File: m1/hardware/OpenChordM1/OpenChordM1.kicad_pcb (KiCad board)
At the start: 4 copper layers, 119 x 63.1 mm, 75 parts, among them J1 TYPE-C-31-M-12, J2 SJ1-3523N (OUT), J3 SJ1-3523N (IN), SW1 SW_Gateron_LP, SW10 EVQPUC02K, SW11 EVQPUC02K, SW13 TS-1187A-B-A-B, SW2 SW_Gateron_LP, SW3 SW_Gateron_LP, SW4 SW_Gateron_LP, SW5 SW_Gateron_LP, SW6 SW_Gateron_LP, SW7 SW_Gateron_LP, SW8 SW_Gateron_LP, SW9 EVQPUC02K, U1 RP2040, U2 CT_Slider_Chev_3_74d5_15_noESD, U3 IQS572-BL-QNR, U4 AT42QT2120-XUR, U5 CT_Trackpad_7x7_37D75, U6 W25Q32JVSSIQ, U7 AP2112K-3.3TRG1, U8 USBLC6-2SC6, U9 TLP2361, Y1 ABM8-272-T3

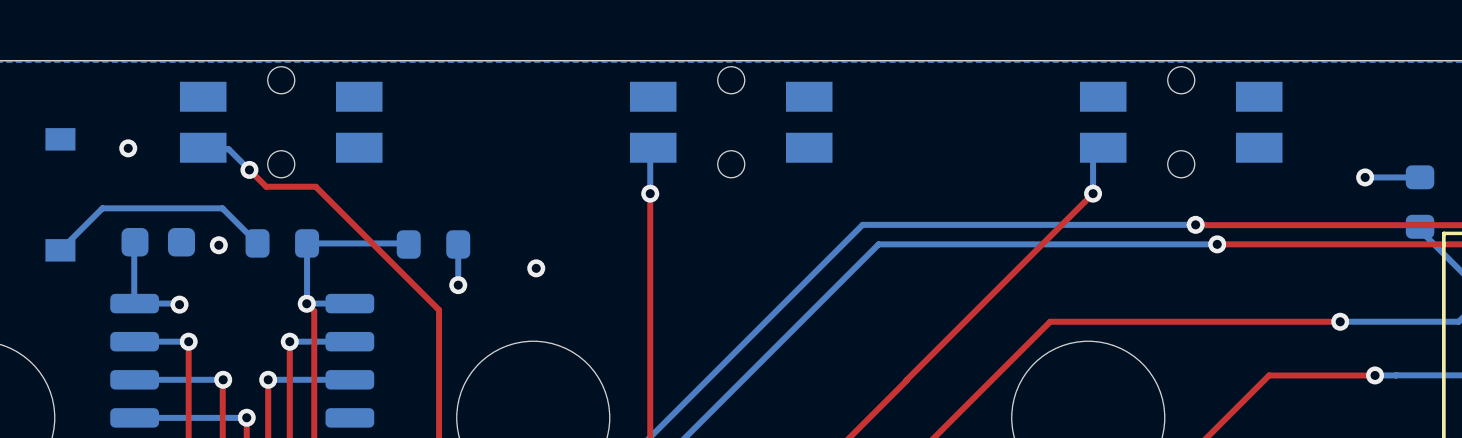
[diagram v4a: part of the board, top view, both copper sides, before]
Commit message: Save USB-C pair routing and a board STEP for the enclosure.
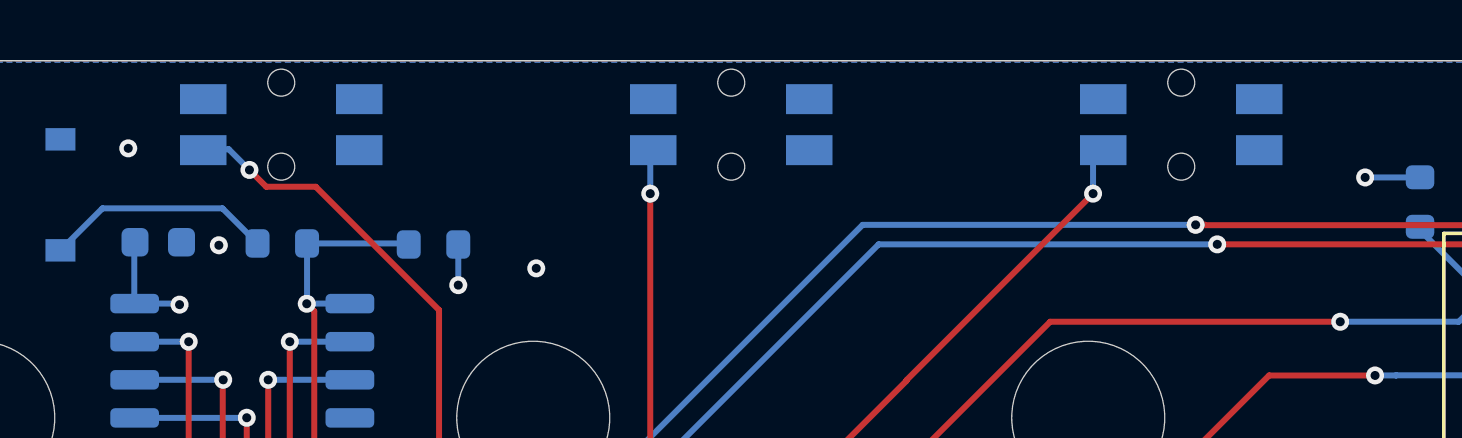
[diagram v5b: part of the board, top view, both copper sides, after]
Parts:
- moved SW10 0.08 mm to (158.6, 48.2)
- moved SW11 0.08 mm to (128.6, 48.2)
- moved SW9 0.08 mm to (143.6, 48.2)
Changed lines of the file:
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@@
 				(font
 					(size 1.27 1.27)
+					(thickness 0.15)
 				)
 				(justify mirror)
@@
 	(footprint "oc-btn:EVQPUC02K"
 		(layer "B.Cu")
-		(at 158.6 48.15)
+		(at 158.6 48.23)
 		(property "Reference" "SW10"
 			(at 0 6.6 180)
@@
 	(footprint "oc-btn:EVQPUC02K"
 		(layer "B.Cu")
-		(at 143.6 48.15)
+		(at 143.6 48.23)
 		(property "Reference" "SW9"
 			(at 0 6.6 180)
@@
 	(footprint "oc-btn:EVQPUC02K"
 		(layer "B.Cu")
-		(at 128.6 48.15)
+		(at 128.6 48.23)
 		(property "Reference" "SW11"
 			(at 0 6.6 180)
@@
 	)
 	(segment
+		(start 107.65 51.63)
+		(end 107.65 52.455)
+		(width 0.2)
+		(layer "B.Cu")
+		(net "Net-(J1-DN1)")
+	)
+	(segment
+		(start 106.65 55.515)
+		(end 106.55 55.615)
+		(width 0.2)
+		(layer "B.Cu")
+		(net "Net-(J1-DN1)")
+	)
+	(segment
+		(start 106.65 52.455)
+		(end 106.65 55.515)
+		(width 0.2)
+		(layer "B.Cu")
+		(net "Net-(J1-DN1)")
+	)
+	(segment
+		(start 106.65 51.63)
+		(end 106.765 51.515)
+		(width 0.2)
+		(layer "B.Cu")
+		(net "Net-(J1-DN1)")
+	)
+	(segment
+		(start 107.535 51.515)
+		(end 107.65 51.63)
+		(width 0.2)
+		(layer "B.Cu")
+		(net "Net-(J1-DN1)")
+	)
+	(segment
+		(start 106.765 51.515)
+		(end 107.535 51.515)
+		(width 0.2)
+		(layer "B.Cu")
+		(net "Net-(J1-DN1)")
+	)
+	(segment
+		(start 106.65 52.455)
+		(end 106.65 51.63)
+		(width 0.2)
+		(layer "B.Cu")
+		(net "Net-(J1-DN1)")
+	)
+	(segment
+		(start 108.45 55.615)
+		(end 108.45 54.215)
+		(width 0.2)
+		(layer "B.Cu")
+		(net "Net-(J1-DP1)")
+	)
+	(segment
+		(start 108.14 52.68)
+		(end 108.14 53.52)
+		(width 0.2)
+		(layer "B.Cu")
+		(net "Net-(J1-DP1)")
+	)
+	(segment
+		(start 107.95 53.71)
+		(end 107.27 53.71)
+		(width 0.2)
+		(layer "B.Cu")
+		(net "Net-(J1-DP1)")
+	)
+	(segment
+		(start 108.14 53.52)
+		(end 107.95 53.71)
+		(width 0.2)
+		(layer "B.Cu")
+		(net "Net-(J1-DP1)")
+	)
+	(segment
+		(start 107.95 53.71)
+		(end 107.95 53.715)
+		(width 0.2)
+		(layer "B.Cu")
+		(net "Net-(J1-DP1)")
+	)
+	(segment
+		(start 107.95 53.715)
+		(end 108.45 54.215)
+		(width 0.2)
+		(layer "B.Cu")
+		(net "Net-(J1-DP1)")
+	)
+	(segment
+		(start 107.14 53.58)
+		(end 107.14 52.68)
+		(width 0.2)
+		(layer "B.Cu")
+		(net "Net-(J1-DP1)")
+	)
+	(segment
+		(start 107.27 53.71)
+		(end 107.14 53.58)
+		(width 0.2)
+		(layer "B.Cu")
+		(net "Net-(J1-DP1)")
+	)
+	(segment
 		(start 108.45 57.89)
 		(end 110.225 57.89)
@@
 	)
 	(segment
+		(start 104.8 54.365)
+		(end 105.745 54.365)
+		(width 0.2)
+		(layer "B.Cu")
+		(net "Net-(J1-CC1)")
+	)
+	(segment
+		(start 105.745 54.365)
+		(end 106.15 53.96)
+		(width 0.2)
+		(layer "B.Cu")
+		(net "Net-(J1-CC1)")
+	)
+	(segment
+		(start 106.15 53.96)
+		(end 106.15 52.455)
+		(width 0.2)
+		(layer "B.Cu")
+		(net "Net-(J1-CC1)")
+	)
+	(segment
+		(start 110.135 54.56)
+		(end 109.129848 53.554848)
+		(width 0.2)
+		(layer "B.Cu")
+		(net "Net-(J1-CC2)")
+	)
+	(segment
+		(start 109.129848 53.554848)
+		(end 109.129848 52.68)
+		(width 0.2)
+		(layer "B.Cu")
+		(net "Net-(J1-CC2)")
+	)
+	(segment
 		(start 132.99 65.77)
 		(end 132.89 65.87)
@@
 		(net "Net-(U1-QSPI_SD1)")
 	)
-	(segment
-		(start 110.135 54.56)
-		(end 109.129848 53.554848)
-		(width 0.2)
-		(layer "B.Cu")
-		(net "Net-(J1-CC2)")
-	)
-	(segment
-		(start 109.129848 53.554848)
-		(end 109.129848 52.68)
-		(width 0.2)
-		(layer "B.Cu")
-		(net "Net-(J1-CC2)")
-	)
-	(segment
-		(start 108.45 55.615)
-		(end 108.45 54.215)
-		(width 0.2)
-		(layer "B.Cu")
-		(net "Net-(J1-DP1)")
-	)
-	(segment
-		(start 108.14 52.68)
-		(end 108.14 53.52)
-		(width 0.2)
-		(layer "B.Cu")
-		(net "Net-(J1-DP1)")
-	)
-	(segment
-		(start 107.95 53.71)
-		(end 107.27 53.71)
-		(width 0.2)
-		(layer "B.Cu")
-		(net "Net-(J1-DP1)")
-	)
-	(segment
-		(start 108.14 53.52)
-		(end 107.95 53.71)
-		(width 0.2)
-		(layer "B.Cu")
-		(net "Net-(J1-DP1)")
-	)
-	(segment
-		(start 107.95 53.71)
-		(end 107.95 53.715)
-		(width 0.2)
-		(layer "B.Cu")
-		(net "Net-(J1-DP1)")
-	)
-	(segment
-		(start 107.95 53.715)
-		(end 108.45 54.215)
-		(width 0.2)
-		(layer "B.Cu")
-		(net "Net-(J1-DP1)")
-	)
-	(segment
-		(start 107.14 53.58)
-		(end 107.14 52.68)
-		(width 0.2)
-		(layer "B.Cu")
-		(net "Net-(J1-DP1)")
-	)
-	(segment
-		(start 107.27 53.71)
-		(end 107.14 53.58)
-		(width 0.2)
-		(layer "B.Cu")
-		(net "Net-(J1-DP1)")
-	)
-	(segment
-		(start 107.65 51.63)
-		(end 107.65 52.455)
-		(width 0.2)
-		(layer "B.Cu")
-		(net "Net-(J1-DN1)")
-	)
-	(segment
-		(start 106.65 55.515)
-		(end 106.55 55.615)
-		(width 0.2)
-		(layer "B.Cu")
-		(net "Net-(J1-DN1)")
-	)
-	(segment
-		(start 106.65 52.455)
-		(end 106.65 55.515)
-		(width 0.2)
-		(layer "B.Cu")
-		(net "Net-(J1-DN1)")
-	)
-	(segment
-		(start 106.65 51.63)
-		(end 106.765 51.515)
-		(width 0.2)
-		(layer "B.Cu")
-		(net "Net-(J1-DN1)")
-	)
-	(segment
-		(start 107.535 51.515)
-		(end 107.65 51.63)
-		(width 0.2)
-		(layer "B.Cu")
-		(net "Net-(J1-DN1)")
-	)
-	(segment
-		(start 106.765 51.515)
-		(end 107.535 51.515)
-		(width 0.2)
-		(layer "B.Cu")
-		(net "Net-(J1-DN1)")
-	)
-	(segment
-		(start 106.65 52.455)
-		(end 106.65 51.63)
-		(width 0.2)
-		(layer "B.Cu")
-		(net "Net-(J1-DN1)")
-	)
-	(segment
-		(start 104.8 54.365)
-		(end 105.745 54.365)
-		(width 0.2)
-		(layer "B.Cu")
-		(net "Net-(J1-CC1)")
-	)
-	(segment
-		(start 105.745 54.365)
-		(end 106.15 53.96)
-		(width 0.2)
-		(layer "B.Cu")
-		(net "Net-(J1-CC1)")
-	)
-	(segment
-		(start 106.15 53.96)
-		(end 106.15 52.455)
-		(width 0.2)
-		(layer "B.Cu")
-		(net "Net-(J1-CC1)")
-	)
 	(zone

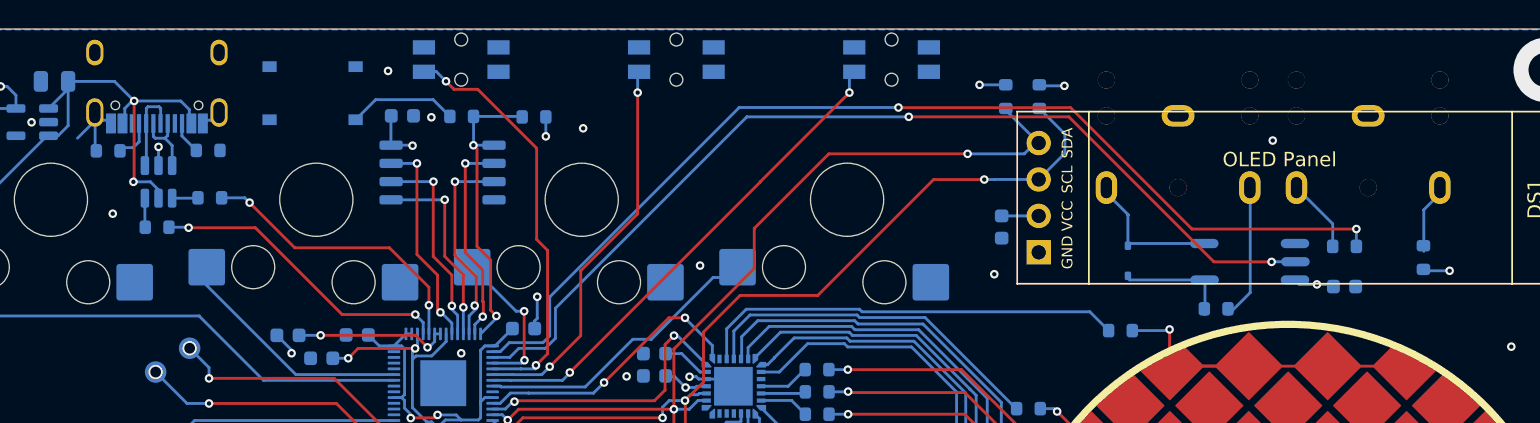
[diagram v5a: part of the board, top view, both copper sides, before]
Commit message: Hang TRS bushings off the board edge and recenter the STEP.
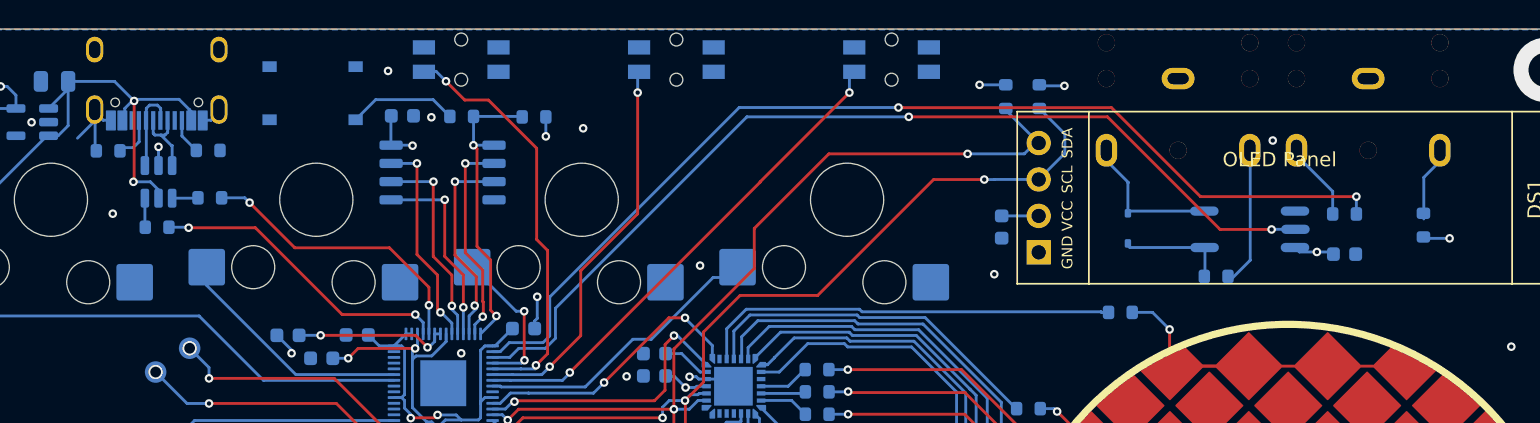
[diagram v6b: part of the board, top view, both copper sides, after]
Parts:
- moved J2 2.60 mm to (191.8, 52.1)
- moved J3 2.60 mm to (178.6, 52.1)
- moved R10 2.26 mm to (181.2, 63.3)
- moved R12 2.26 mm to (195.7, 59.8)
- moved C6 2.26 mm to (190.2, 61.8)
- moved D1 2.26 mm to (175.1, 60.0)
- moved R11 2.26 mm to (190.2, 59.0)
- moved U9 2.26 mm to (183.6, 60.1)
- moved R16 1.27 mm to (174.6, 65.8)
- moved J1 0.21 mm to (107.4, 50.0)
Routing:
- net /GPIO1: track 69.0 -> 68.1 mm
- net /GPIO0: track 73.9 -> 73.0 mm
- net Net-(J3-Tip): track 9.08 -> 10.0 mm
- net VBUS: track 36.1 -> 37.0 mm
- net Net-(D1-A): track 9.67 -> 10.4 mm
- net Net-(U5-Rx1): track 11.1 -> 11.6 mm
- net Net-(U3-Rx0): track 29.9 -> 29.4 mm
